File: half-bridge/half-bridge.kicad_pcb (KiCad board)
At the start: 4 copper layers, 59 x 36 mm, 69 parts, among them J1 Conn_01x11_Pin, J3 Conn_01x11_Pin, J4 Conn_01x11_Pin, J5 Conn_01x11_Pin, J6 Conn_01x11_Pin, Q1 EPC2306, Q2 EPC2306, U1 LMG1210, U2 INA293B

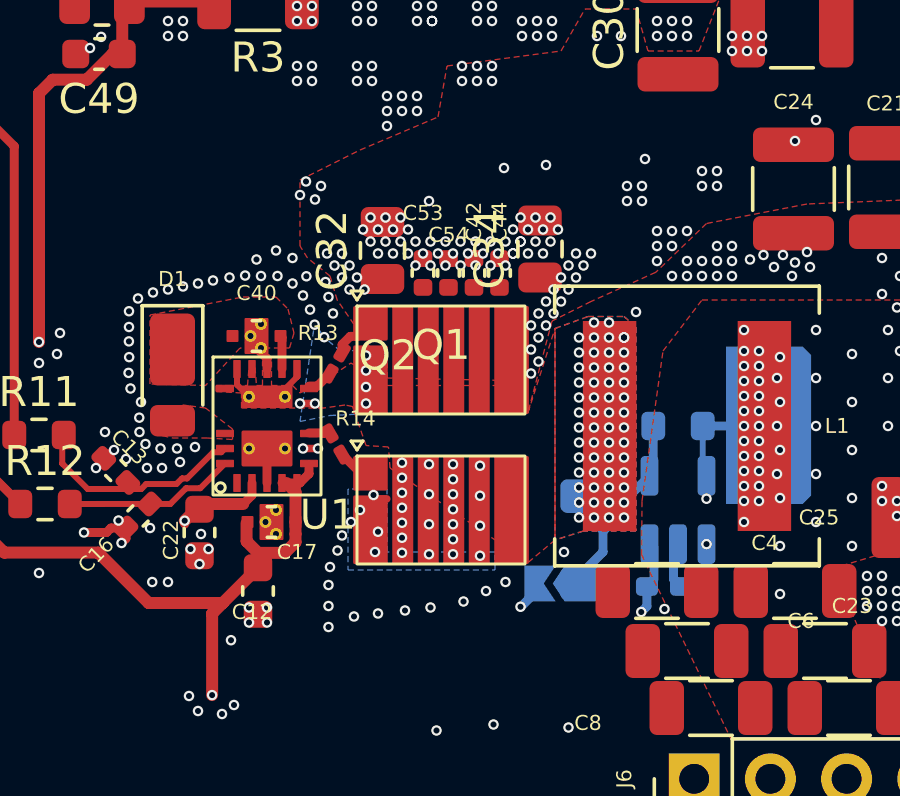
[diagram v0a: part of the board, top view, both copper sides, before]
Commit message: Further layout improvements
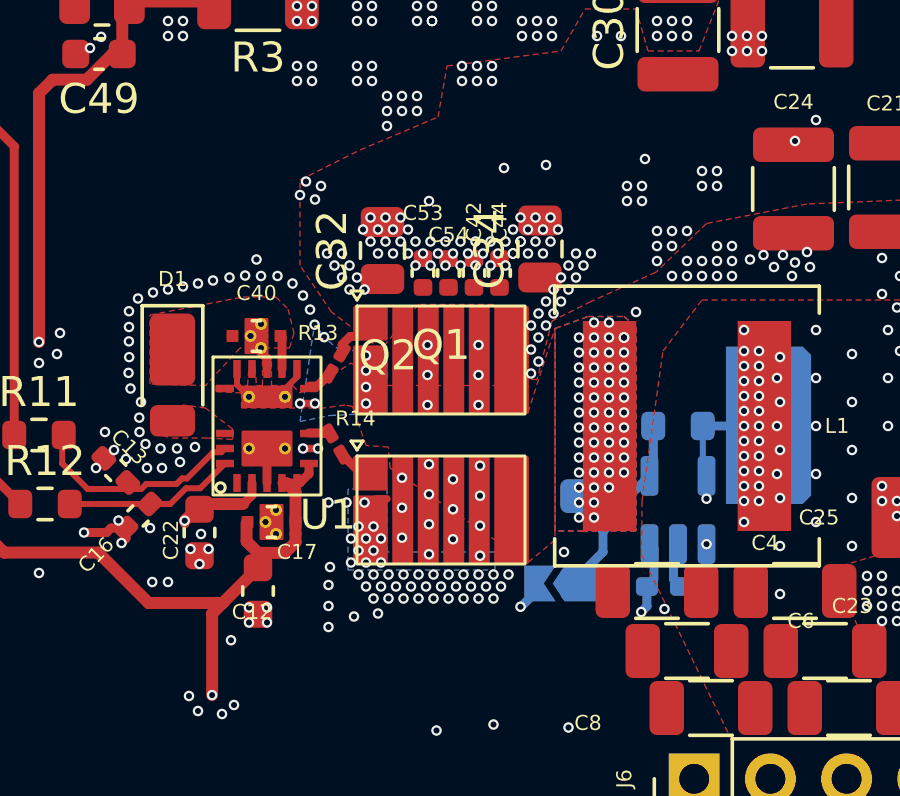
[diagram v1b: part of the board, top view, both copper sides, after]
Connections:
- C42 pad 1: Net-(C42-Pad1) -> POWER_HIGH
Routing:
- net Switch_node: track 3.62 -> 3.92 mm, vias 75 -> 68
- net 0: vias 414 -> 439

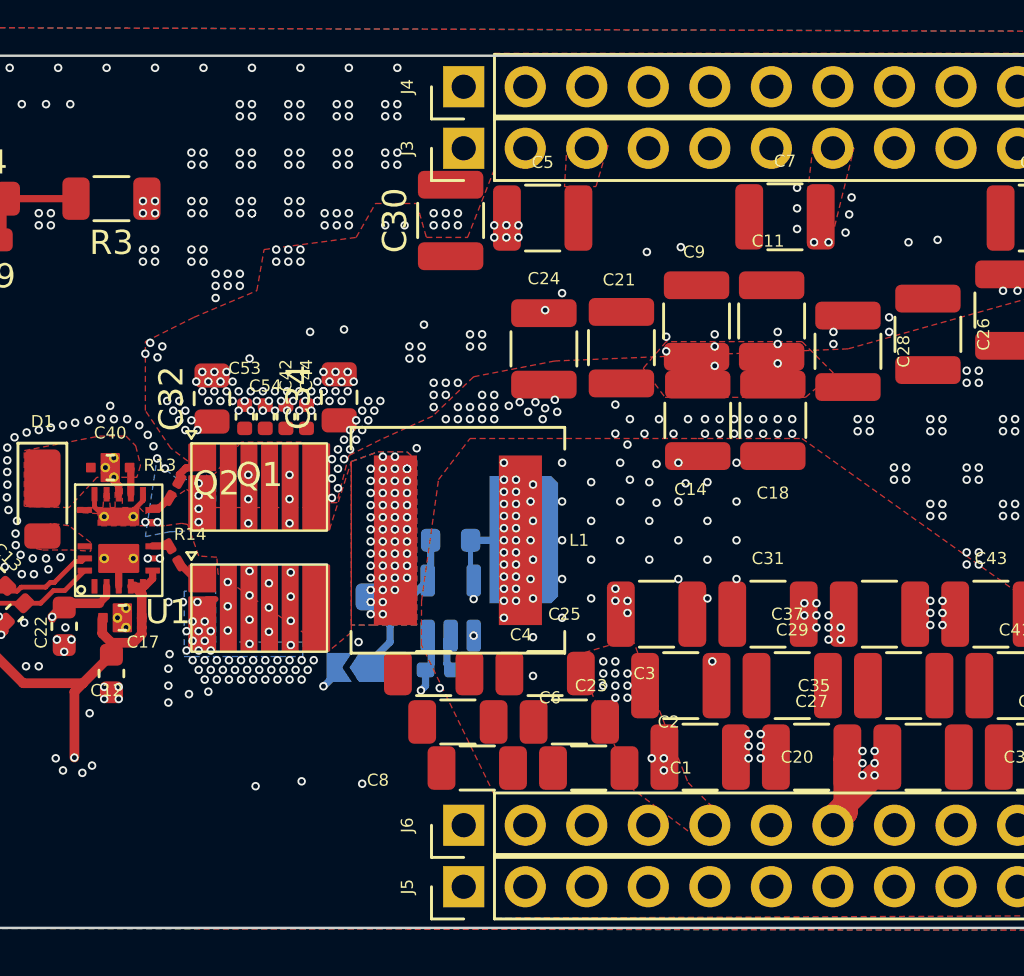
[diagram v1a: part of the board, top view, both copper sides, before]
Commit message: Clean up overlapping vias and zones
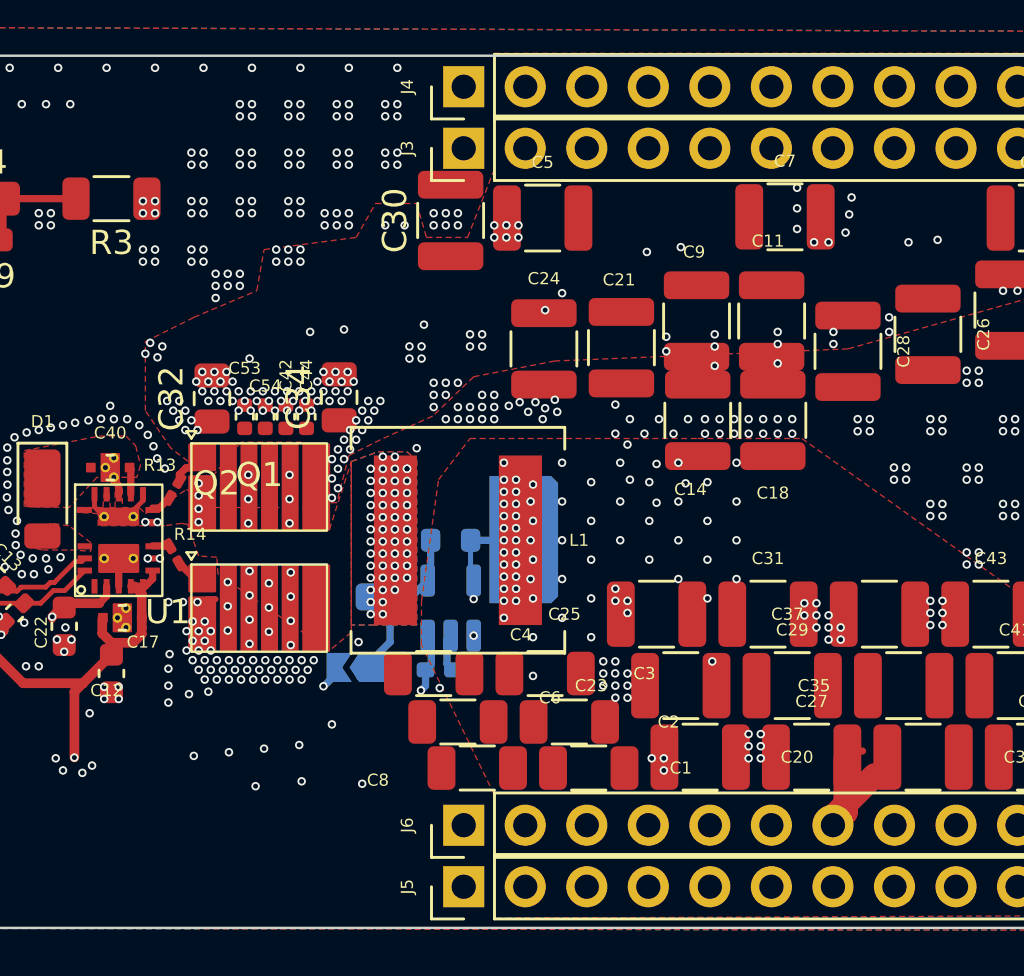
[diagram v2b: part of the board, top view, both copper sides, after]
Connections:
- L1 pad 2: Net-(L1-Pad2) -> POWER_LOW
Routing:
- net 0: track 11.9 -> 12.5 mm, vias 439 -> 435

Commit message: More changes
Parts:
- removed C1, C2, C3, C4, C6, C8: 220nF, Capacitor_SMD:C_1206_3216Metric
- moved C19 27.4 mm to (137.8, 85.2), turned to 180 degrees
- moved C41 27.2 mm to (138.1, 109.8), turned to 180 degrees
- moved C28 26.0 mm to (132.2, 91.2), turned to 0 degrees
- moved C43 25.7 mm to (138.5, 106.5), turned to 180 degrees
- moved C26 24.3 mm to (137.3, 88.2), turned to 0 degrees
- moved C21 18.9 mm to (131.2, 85.2), turned to 0 degrees
- moved C24 14.4 mm to (131.7, 88.2), turned to 180 degrees
- moved C30 6.51 mm to (136.8, 91.2), turned to 180 degrees
- moved R3 3.10 mm to (124.6, 85.9)
- moved R4 2.45 mm to (120.0, 85.9)
- moved C49 2.25 mm to (120.2, 87.6)
- moved C34 0.29 mm to (136.9, 94.3)
- moved C32 0.28 mm to (132.1, 94.3)
- moved C53 0.25 mm to (133.4, 94.9)
- moved C44 0.20 mm to (135.6, 94.9)
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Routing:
- net FB_HIGH: track 30.2 -> 29.6 mm
- net POWER_HIGH: vias 84 -> 114
- net 0: vias 435 -> 390

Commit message: More changes
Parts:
- added H1: WE 97730256330, Mounting_Wuerth:Mounting_Wuerth_WA-SMSI-M1.6_H2.5mm_ThreadDepth1.5mm_NoNPTH_97730256330, F.Cu at (124.0, 92.0)
- added H2: WE 97730256330, Mounting_Wuerth:Mounting_Wuerth_WA-SMSI-M1.6_H2.5mm_ThreadDepth1.5mm_NoNPTH_97730256330, F.Cu at (146.0, 92.0)
- added H3: WE 97730256330, Mounting_Wuerth:Mounting_Wuerth_WA-SMSI-M1.6_H2.5mm_ThreadDepth1.5mm_NoNPTH_97730256330, F.Cu at (124.0, 109.0)
- added H4: WE 97730256330, Mounting_Wuerth:Mounting_Wuerth_WA-SMSI-M1.6_H2.5mm_ThreadDepth1.5mm_NoNPTH_97730256330, F.Cu at (134.0, 109.0)
- added H5: WE 97730256330, Mounting_Wuerth:Mounting_Wuerth_WA-SMSI-M1.6_H2.5mm_ThreadDepth1.5mm_NoNPTH_97730256330, F.Cu at (146.0, 108.0)
- added J2: MountingHole_Pad, Connector_Wire:SolderWirePad_1x01_SMD_5x10mm, B.Cu at (163.6, 90.4)
- added J7: MountingHole_Pad, Connector_Wire:SolderWirePad_1x01_SMD_5x10mm, F.Cu at (163.6, 90.4)
- added J8: MountingHole_Pad, Connector_Wire:SolderWirePad_1x01_SMD_5x10mm, B.Cu at (163.6, 98.9)
- added J9: MountingHole_Pad, Connector_Wire:SolderWirePad_1x01_SMD_5x10mm, F.Cu at (163.6, 98.9)
- moved C15 15.4 mm to (150.5, 86.7)
- moved C48 0.15 mm to (141.2, 105.2)
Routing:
- net 0: track 12.5 -> 12.4 mm, vias 390 -> 370
- net POWER_HIGH: vias 114 -> 112
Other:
- board text added: "GND"
- board text added: "HI+"
- board text added: "LO+"

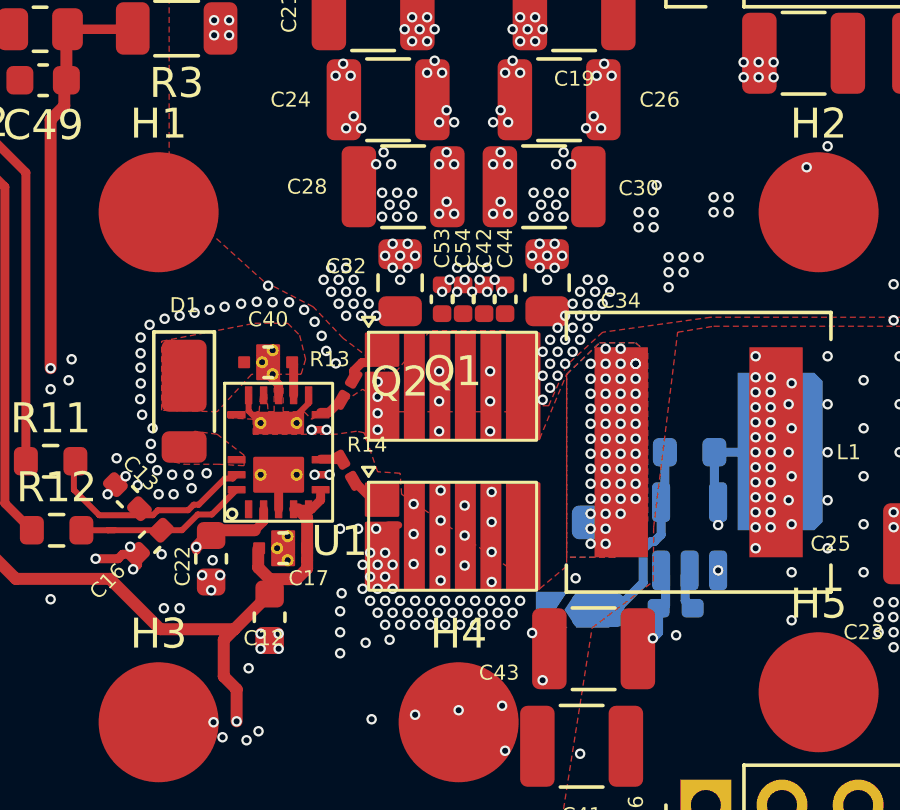
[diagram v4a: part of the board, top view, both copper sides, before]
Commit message: Add some more small cap
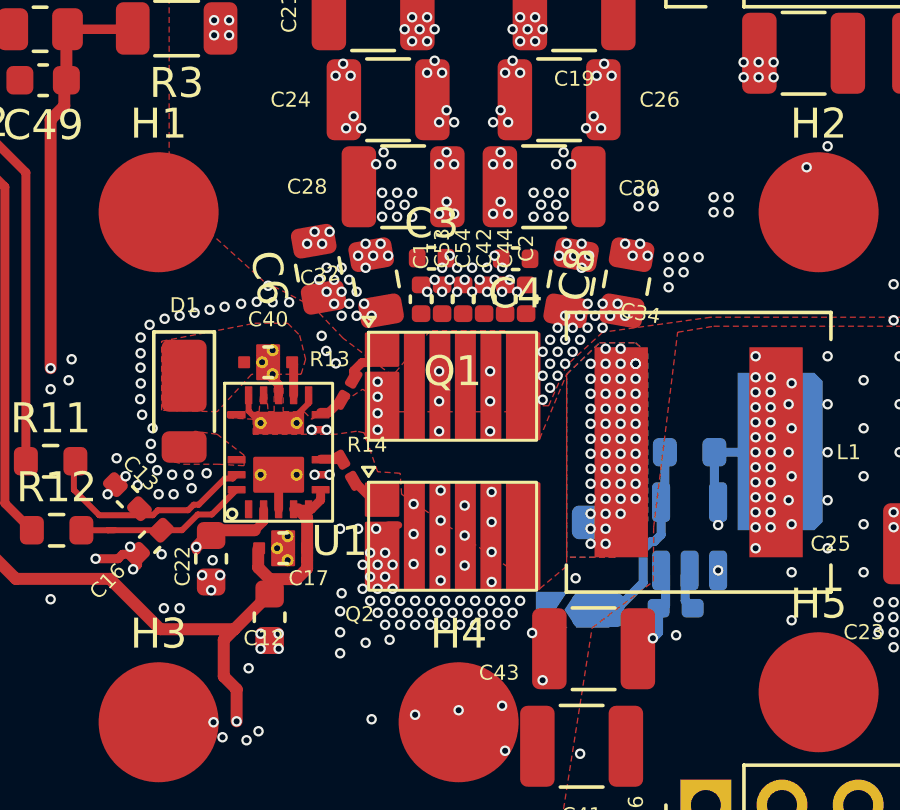
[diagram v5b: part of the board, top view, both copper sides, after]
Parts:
- added C1: cap=1nF esr=72m srf=304MEG, Capacitor_SMD:C_0402_1005Metric, F.Cu at (132.8, 94.9)
- added C2: cap=1nF esr=72m srf=304MEG, Capacitor_SMD:C_0402_1005Metric, F.Cu at (136.2, 94.9)
- added C3: cap=1nF esr=72m srf=304MEG, Capacitor_SMD:C_0402_1005Metric, F.Cu at (133.1, 93.5)
- added C4: cap=1nF esr=72m srf=304MEG, Capacitor_SMD:C_0402_1005Metric, F.Cu at (135.9, 93.5)
- added C6: 10nF, Capacitor_SMD:C_0805_2012Metric, F.Cu at (129.3, 93.9)
- added C8: 10nF, Capacitor_SMD:C_0805_2012Metric, F.Cu at (139.6, 94.3)
- C32, C34: value ?nF -> 10nF
- R3: value R -> 100k
- R4: value R -> 10k
- moved C32 0.80 mm to (131.2, 94.3), turned to 100 degrees
- moved C34 0.80 mm to (137.8, 94.3), turned to 80 degrees
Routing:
- net POWER_HIGH: vias 112 -> 110
- net 0: vias 370 -> 379

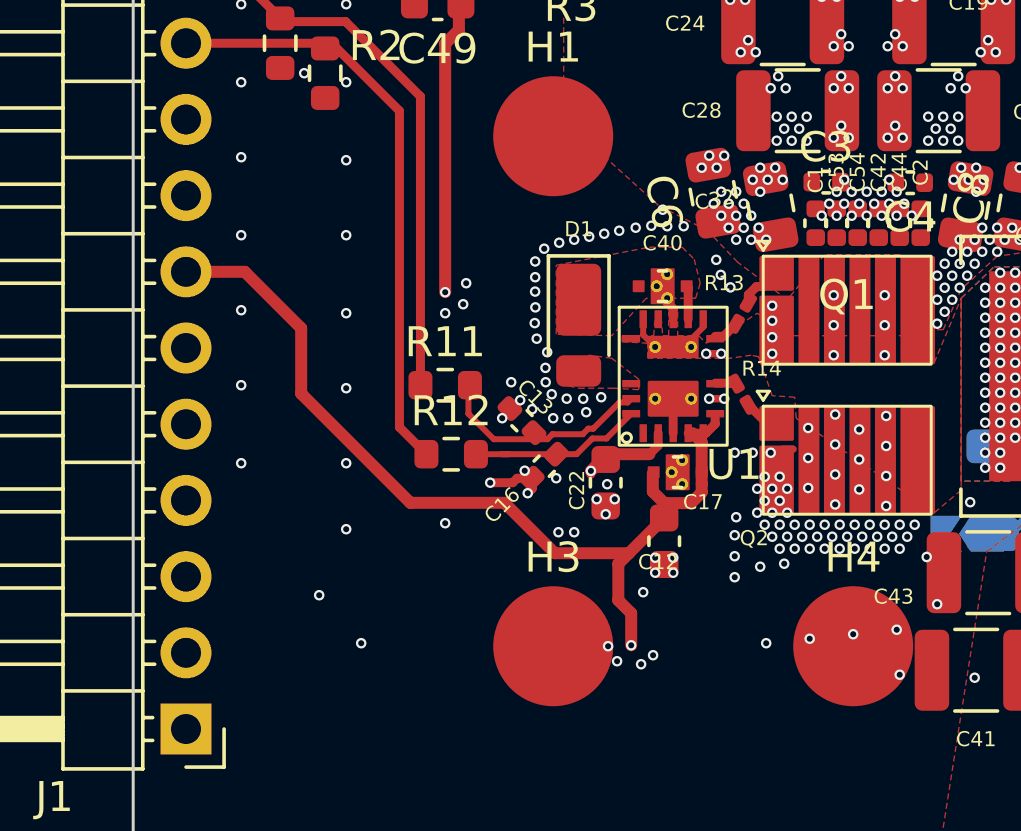
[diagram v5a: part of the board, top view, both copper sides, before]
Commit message: Add NTC
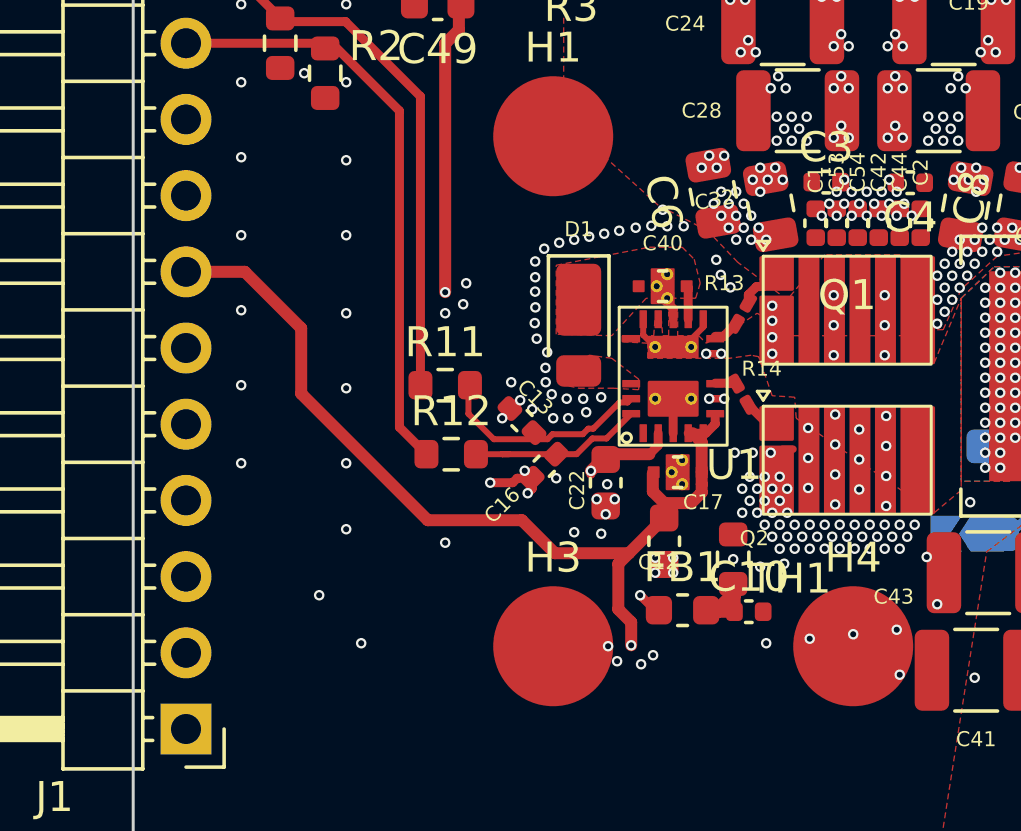
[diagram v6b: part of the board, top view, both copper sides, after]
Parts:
- added C10: 100nF, Capacitor_SMD:C_0402_1005Metric, F.Cu at (130.5, 107.8)
- added FB1: FerriteBead, Inductor_SMD:L_0603_1608Metric, F.Cu at (128.3, 107.8)
- added TH1: Thermistor_NTC, Resistor_SMD:R_0603_1608Metric, F.Cu at (130.0, 106.1)
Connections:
- J1 pad 7: +5V -> NTC
- J1 pad 8: 0 -> +5V
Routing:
- net NTC: track 0.00 -> 25.9 mm, vias 0 -> 1
- net Net-(C10-Pad1): track 0.00 -> 3.38 mm
